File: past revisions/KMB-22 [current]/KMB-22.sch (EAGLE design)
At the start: 140 parts, among them J1 503182-1852, J2 10118194-0001LF, J3 DCJ0303, Q1 IRLML2803, Q10 IRLML5103, Q11 IRLML5103, Q12 IRLML5103, Q13 IRLML5103, Q14 IRLML2803, Q15 IRLML2803, Q16 IRLML5103, Q2 IRLML2803, Q5 IRLML2803, Q6 IRLML2803, Q7 IRLML2803, Q8 IRLML2803, Q9 IRLML5103, U1 MAX706R, U12 EP2W+, U13 RFM23BP, U14 S1216V8, U15 XTB_2018_07_15, U16 XTB_2018_07_15, U17 XTB_2018_07_15, U18 XTB_2018_07_15, U2 FXAS21002FXAS21002, U20 MR25H40MDF, U3 LSM9DS1, U4 ATSAMD21G-A, U5 MAX4372TEUK+T, U6 LTC4121-4.2, U7 TPS54226PWPRPWP14_2P31X2P46-L, U8 PE014006, U9 PE014006, X1 BU-SMA-V, X2 BU-SMA-V, X3 BU-SMA-V, Y1 32.768kHz

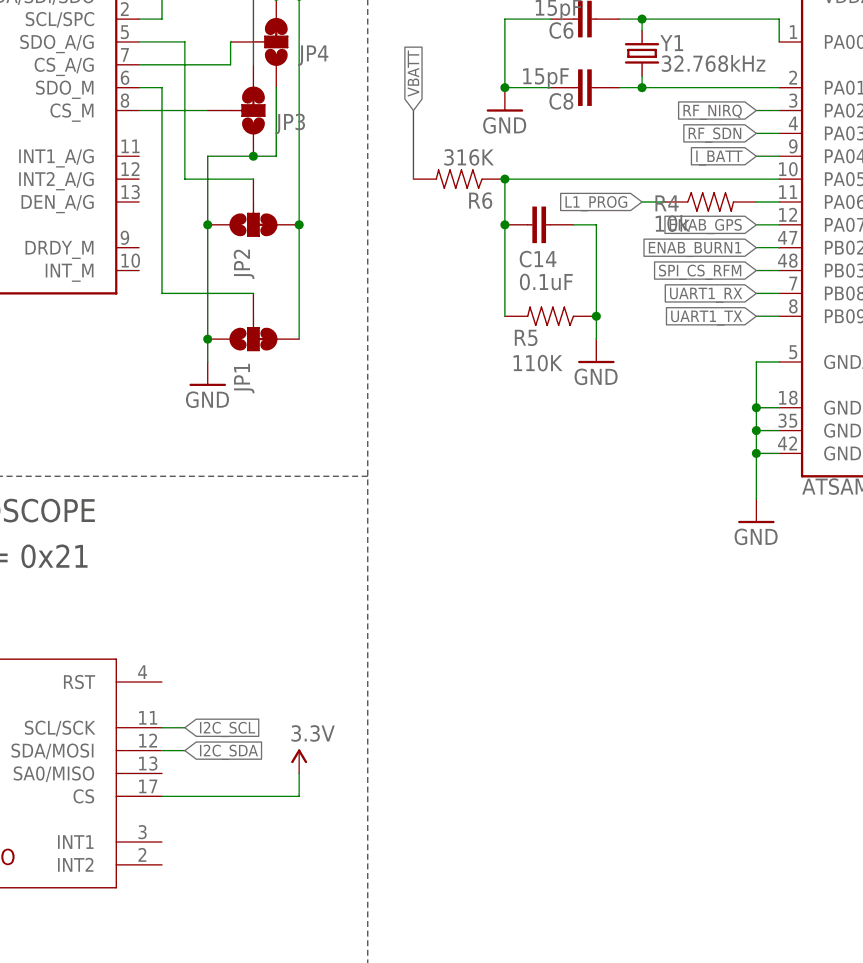
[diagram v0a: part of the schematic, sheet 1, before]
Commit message: changed solar panel connector on KMB-22
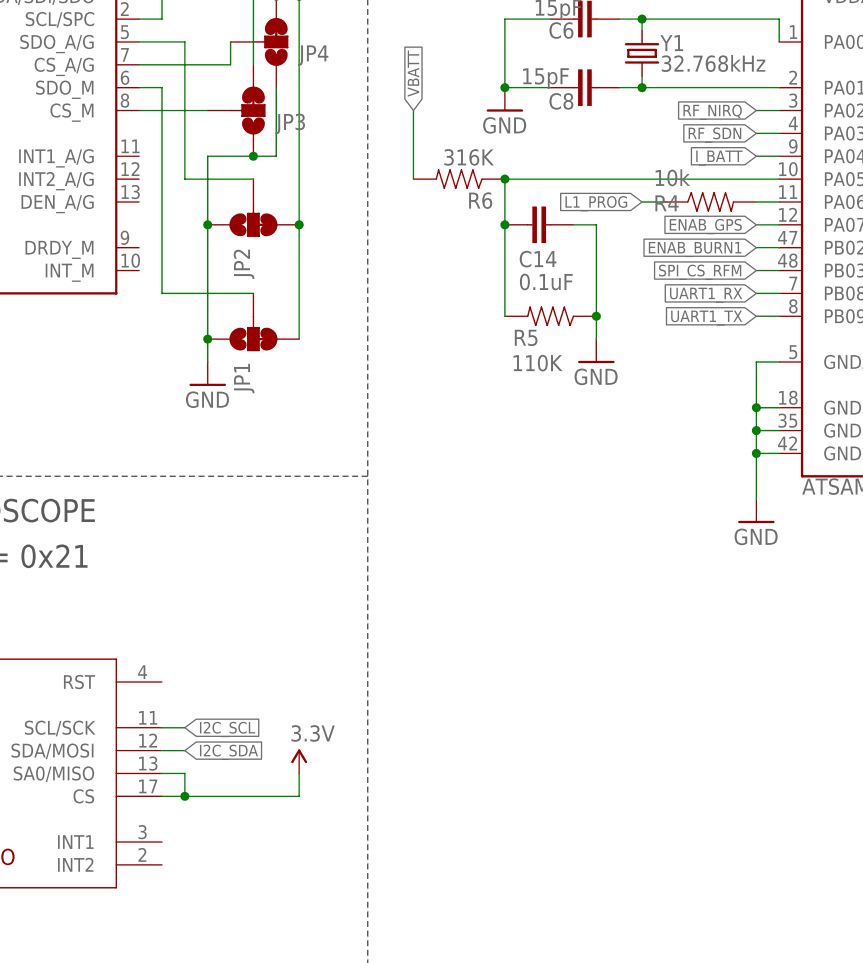
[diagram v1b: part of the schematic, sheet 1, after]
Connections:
- net 3.3V: now also U2.SA0/MISO
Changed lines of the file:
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@@
 <instance part="R4" gate="G$1" x="127" y="88.9" smashed="yes">
 <attribute name="NAME" x="120.65" y="87.8586" size="1.778" layer="95"/>
-<attribute name="VALUE" x="120.65" y="85.598" size="1.778" layer="96"/>
+<attribute name="VALUE" x="120.65" y="90.678" size="1.778" layer="96"/>
 </instance>
 <instance part="C11" gate="G$1" x="175.26" y="144.78"/>
@@
 <wire x1="81.28" y1="22.86" x2="81.28" y2="25.4" width="0.1524" layer="91"/>
 <pinref part="U2" gate="G$1" pin="CS"/>
-<wire x1="66.04" y1="22.86" x2="81.28" y2="22.86" width="0.1524" layer="91"/>
+<wire x1="66.04" y1="22.86" x2="68.58" y2="22.86" width="0.1524" layer="91"/>
+<pinref part="U2" gate="G$1" pin="SA0/MISO"/>
+<wire x1="68.58" y1="22.86" x2="81.28" y2="22.86" width="0.1524" layer="91"/>
+<wire x1="66.04" y1="25.4" x2="68.58" y2="25.4" width="0.1524" layer="91"/>
+<wire x1="68.58" y1="25.4" x2="68.58" y2="22.86" width="0.1524" layer="91"/>
+<junction x="68.58" y="22.86"/>
 </segment>
 </net>
